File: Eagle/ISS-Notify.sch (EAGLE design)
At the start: 56 parts, among them J2 JST2, J3 PROTOSPACE2, SW1 9077-1, SW2 SWITCH, U1 ATMEGA32U4, U2 MCP7940N, U3 TPS63001, U4 MCP73811, U5 TLC5971, U6 TLC5971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

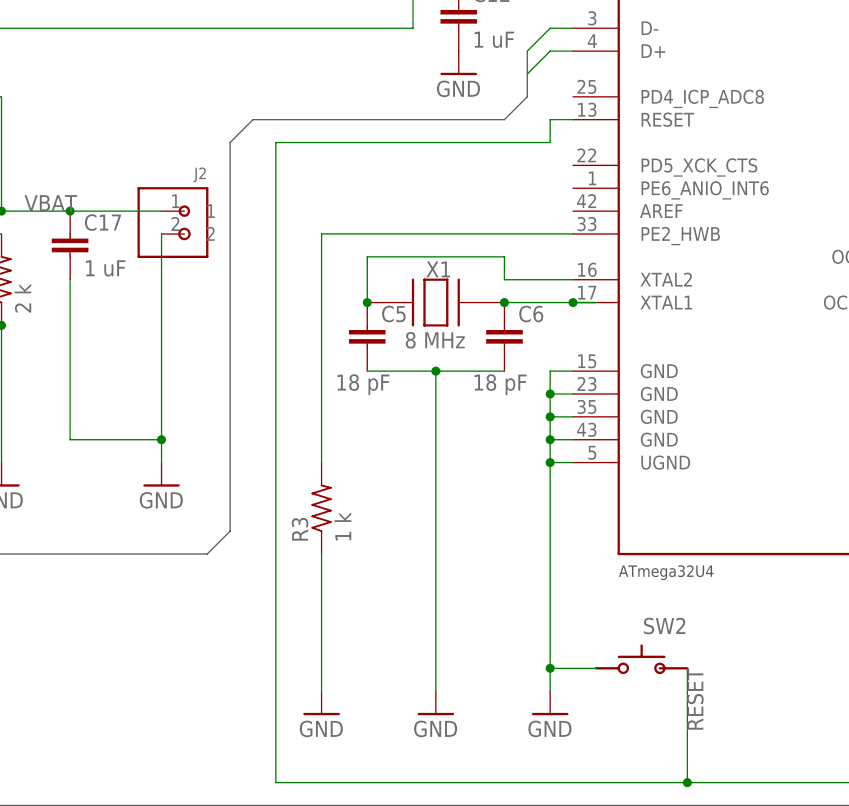
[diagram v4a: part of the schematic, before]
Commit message: names of J2 and reset button so they show up logicall on screenprint
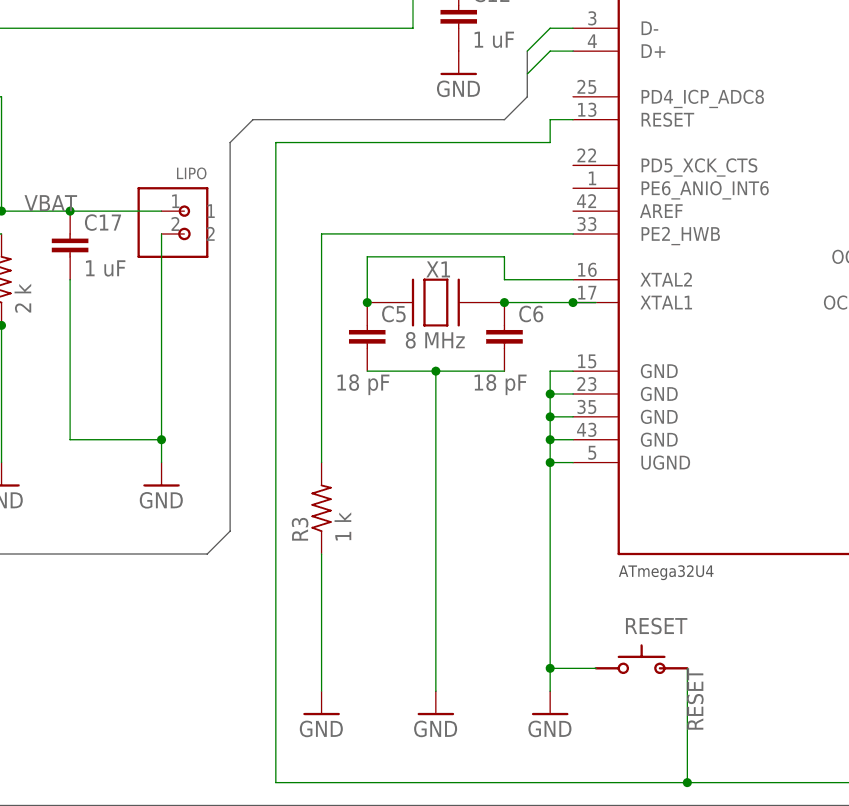
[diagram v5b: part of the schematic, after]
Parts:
- renumbered J2 to LIPO, SW2 to RESET
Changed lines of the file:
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@@
 <?xml version="1.0" encoding="utf-8"?>
 <!DOCTYPE eagle SYSTEM "eagle.dtd">
-<eagle version="6.3">
+<eagle version="6.4">
 <drawing>
 <settings>
@@
 <part name="P+4" library="supply1" deviceset="VCC" device=""/>
 <part name="GND16" library="supply1" deviceset="GND" device=""/>
-<part name="J2" library="ISS-Notify" deviceset="JST2" device=""/>
+<part name="LIPO" library="ISS-Notify" deviceset="JST2" device=""/>
 <part name="GND17" library="supply1" deviceset="GND" device=""/>
 <part name="U5" library="ISS-Notify" deviceset="TLC5971" device=""/>
@@
 <part name="P+9" library="supply1" deviceset="VCC" device=""/>
 <part name="FRAME1" library="frames" deviceset="A3L-LOC" device="" value="ISS Notify"/>
-<part name="SW2" library="ISS-Notify" deviceset="SWITCH" device=""/>
+<part name="RESET" library="ISS-Notify" deviceset="SWITCH" device=""/>
 <part name="U$1" library="ISS-Notify" deviceset="_4-BARE_MOUNTING_HOLE" device="/.300"/>
 <part name="U$2" library="ISS-Notify" deviceset="_4-BARE_MOUNTING_HOLE" device="/.300"/>
@@
 <instance part="P+4" gate="VCC" x="231.14" y="149.86"/>
 <instance part="GND16" gate="1" x="198.12" y="111.76"/>
-<instance part="J2" gate="G$1" x="106.68" y="170.18" rot="MR0"/>
+<instance part="LIPO" gate="G$1" x="106.68" y="170.18" rot="MR0"/>
 <instance part="GND17" gate="1" x="104.14" y="142.24"/>
 <instance part="U5" gate="G$1" x="111.76" y="48.26"/>
@@
 <instance part="P+9" gate="VCC" x="299.72" y="157.48"/>
 <instance part="FRAME1" gate="G$1" x="0" y="0"/>
-<instance part="SW2" gate="G$1" x="157.48" y="121.92" rot="MR0"/>
+<instance part="RESET" gate="G$1" x="157.48" y="121.92" rot="MR0"/>
 <instance part="U$1" gate="MT" x="22.86" y="58.42"/>
 <instance part="U$2" gate="MT" x="22.86" y="50.8"/>
@@
 <wire x1="149.86" y1="152.4" x2="147.32" y2="152.4" width="0.1524" layer="91"/>
 <junction x="147.32" y="152.4"/>
-<pinref part="SW2" gate="G$1" pin="2"/>
+<pinref part="RESET" gate="G$1" pin="2"/>
 <wire x1="152.4" y1="121.92" x2="147.32" y2="121.92" width="0.1524" layer="91"/>
 <junction x="147.32" y="121.92"/>
@@
 </segment>
 <segment>
-<pinref part="J2" gate="G$1" pin="2"/>
+<pinref part="LIPO" gate="G$1" pin="2"/>
 <wire x1="104.14" y1="170.18" x2="104.14" y2="147.32" width="0.1524" layer="91"/>
 <pinref part="GND17" gate="1" pin="GND"/>
@@
 <pinref part="D1" gate="G$1" pin="A"/>
 <wire x1="86.36" y1="185.42" x2="71.12" y2="185.42" width="0.1524" layer="91"/>
-<pinref part="J2" gate="G$1" pin="1"/>
+<pinref part="LIPO" gate="G$1" pin="1"/>
 <wire x1="86.36" y1="172.72" x2="93.98" y2="172.72" width="0.1524" layer="91"/>
 <junction x="86.36" y="172.72"/>
@@
 <pinref part="U1" gate="ATMEGA" pin="RESET"/>
 <wire x1="147.32" y1="182.88" x2="149.86" y2="182.88" width="0.1524" layer="91"/>
-<pinref part="SW2" gate="G$1" pin="1"/>
+<pinref part="RESET" gate="G$1" pin="1"/>
 <wire x1="162.56" y1="121.92" x2="162.56" y2="109.22" width="0.1524" layer="91"/>
 <junction x="162.56" y="109.22"/>
